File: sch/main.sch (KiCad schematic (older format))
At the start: 0 parts

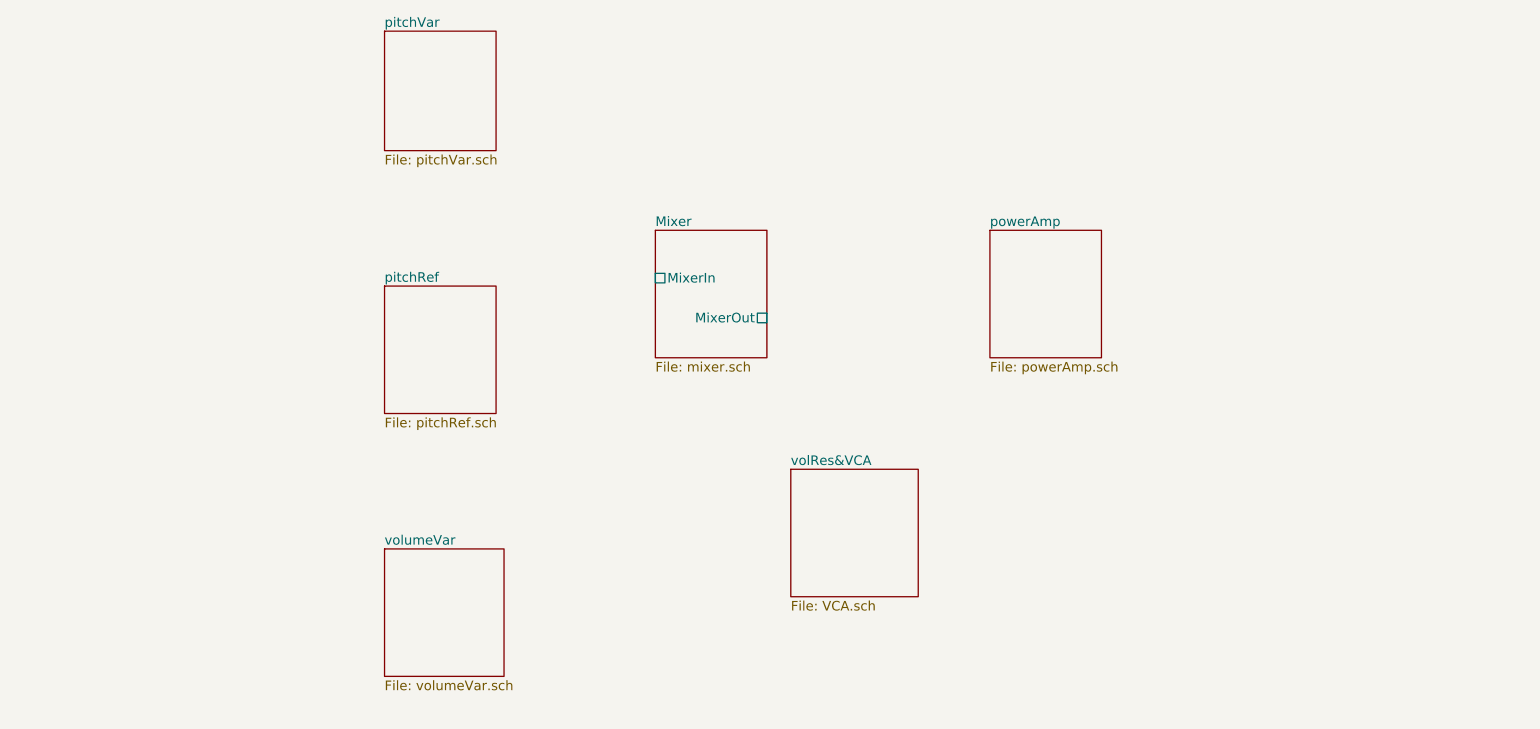
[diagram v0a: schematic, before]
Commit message: Implementados osciladores de tom (de referência e variável) e volume, circuito ressonante de volume e amplificador controlado por tensão (VCA)
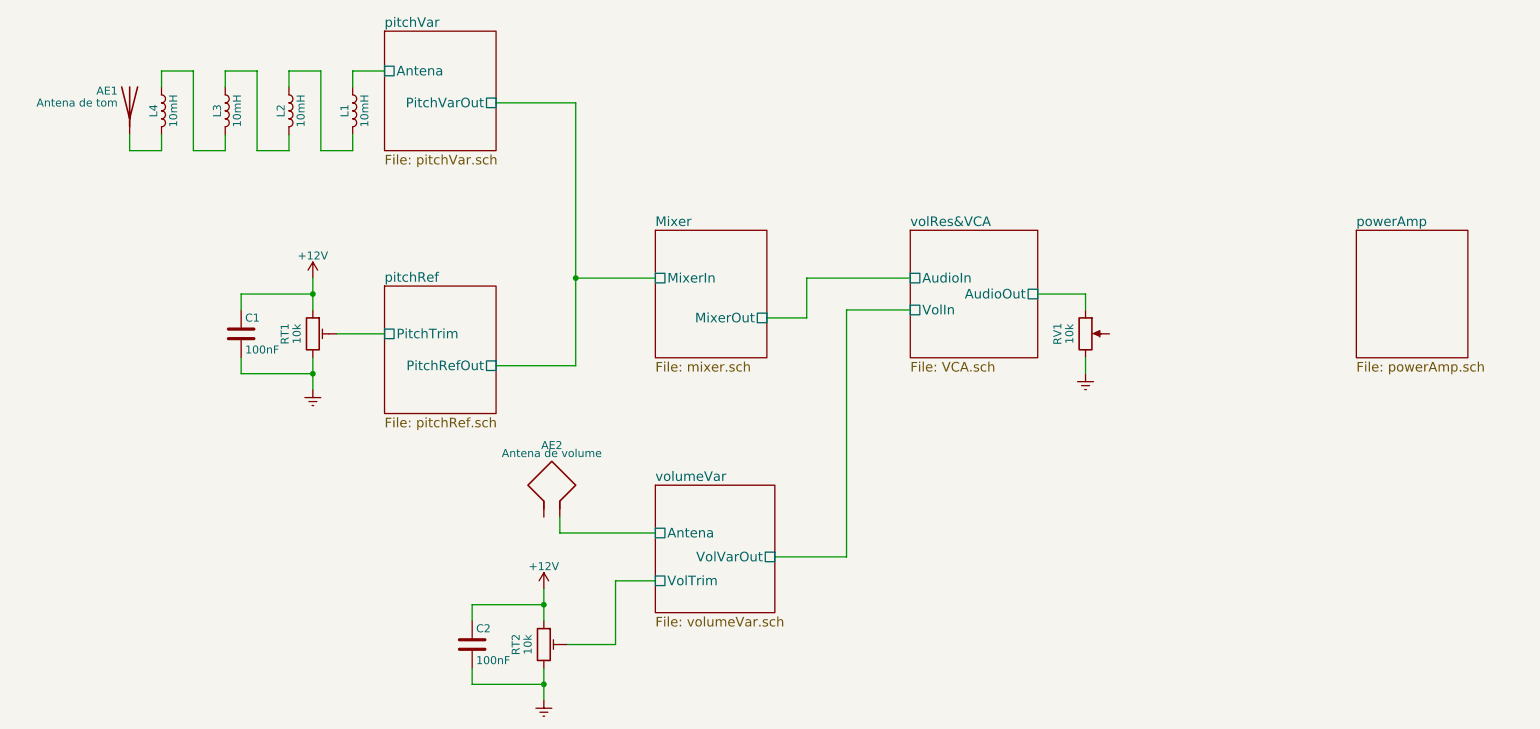
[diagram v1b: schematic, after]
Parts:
- added AE1: Antena de tom, symbol Antenna
- added AE2: Antena de volume, symbol Antenna_Loop
- added C1, C2: 100nF, symbol C
- added L1, L2, L3, L4: 10mH, symbol L
- added RT1, RT2: 10k, symbol POT_TRIM
- added RV1: 10k, symbol POT
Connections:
- new net: L1.2, L2.1
- new net: L2.2, L3.1
- new net: L3.2, L4.1
- new net: AE1.1 (A), L4.2
- new net +12V: C1.1, C2.1, RT1.1, RT2.1
- new net GNDREF: C1.2, C2.2, RT1.3, RT2.3, RV1.3
- new net pitchRef/PitchTrim: RT1.2
- new net pitchVar/Antena: L1.1
- new net volRes&VCA/AudioOut: RV1.1
- new net volumeVar/Antena: AE2.2
- new net volumeVar/VolTrim: RT2.2
